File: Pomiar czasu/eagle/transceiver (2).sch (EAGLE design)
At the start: 64 parts, among them IC1 MEGA8-AI, IC2 LF33, IC3 LF50, U1 RFM69HW

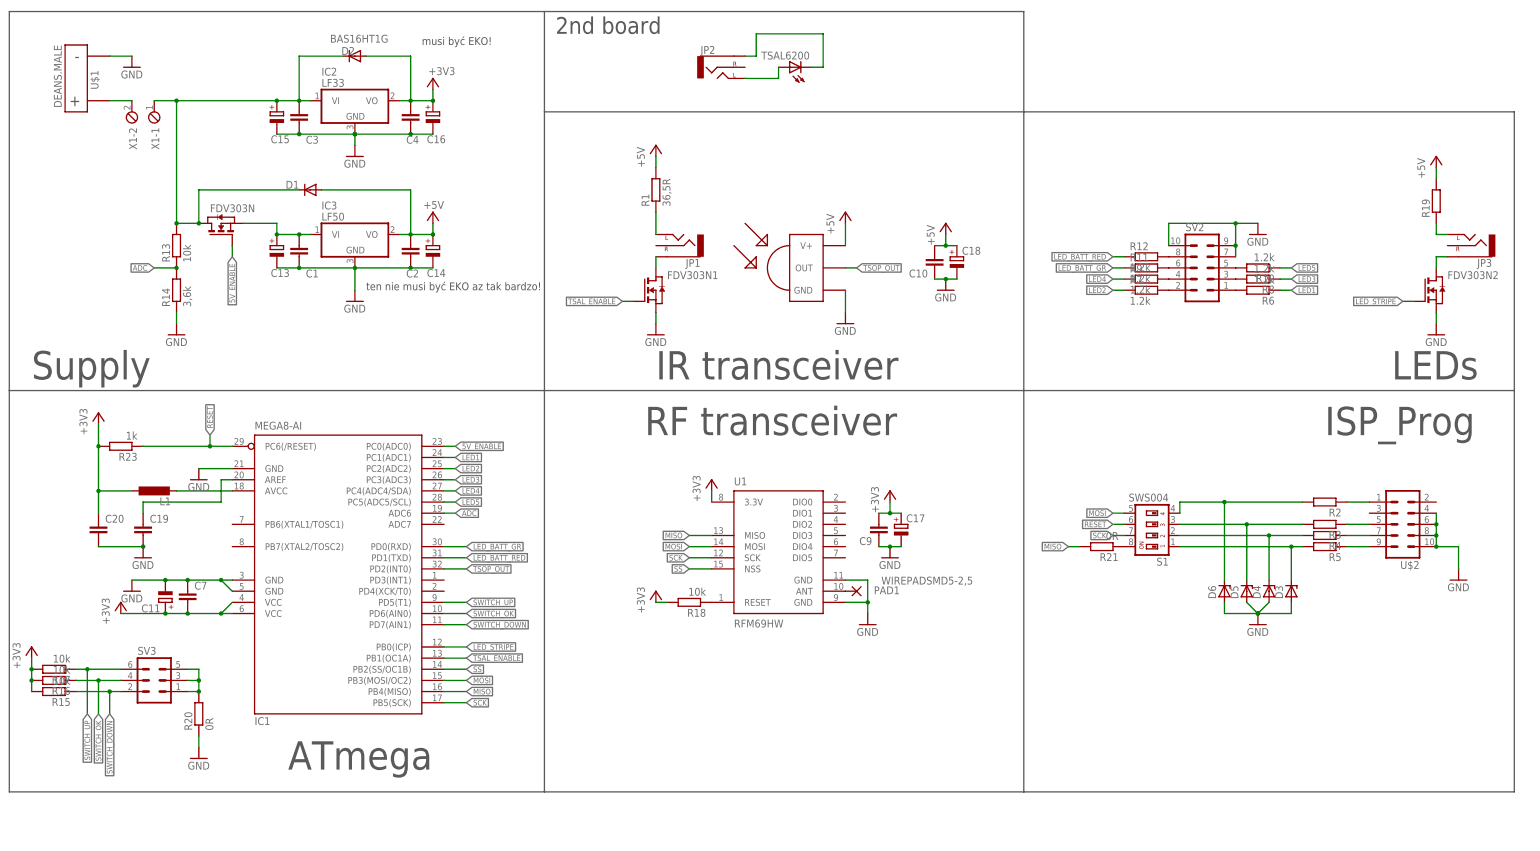
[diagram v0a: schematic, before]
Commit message: RFM69:communication master->sensor works!
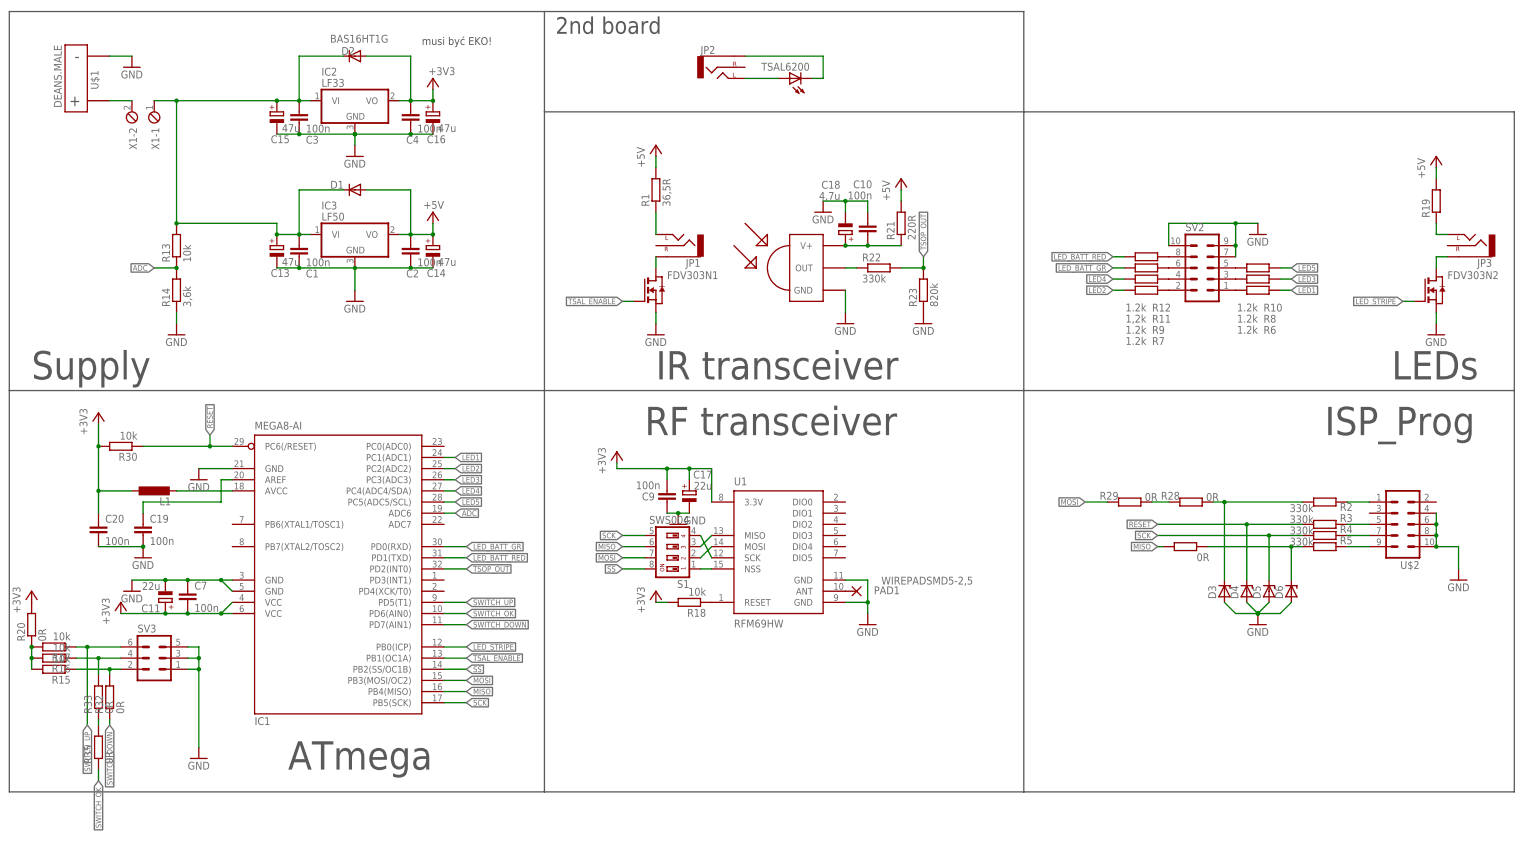
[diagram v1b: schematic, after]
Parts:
- removed FDV303N: (no value), zetex:NMOSSOT23
- added R22: 330k, resistor:R-EU_R0805
- added R28, R29, R31, R32, R33, R35: 0R, rcl:R-EU_R1206
- added R30: 10k, resistor:R-EU_R0805
- C1, C10, C19, C2, C20, C3, C4, C7, C9: value (none) -> 100n
- C11, C17: value (none) -> 22u
- C13, C14, C15, C16: value (none) -> 47u
- C18: value (none) -> 4,7u
- R2, R3, R4, R5: value (none) -> 330k
- R21: value 0R -> 220R; device rcl:R-EU_R1206 -> resistor:R-EU_R0805
- R23: value 1k -> 820k
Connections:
- removed net 5V_ENABLE: FDV303N.G, IC1.PC0(ADC0)
- removed net N$24: R21.1, S1.8
- new net N$25: C10.1, C18.+, R21.1, TSOP.V+
- new net N$33: R16.1, R33.2, SV3.4
- new net N$35: R33.1, R35.2
- new net N$36: S1.3, U1.MISO
- new net N$37: S1.2, U1.MOSI
- new net N$38: S1.4, U1.SCK
- new net N$39: S1.1, U1.NSS
- net +3V3: now also R20.2, R30.2; no longer R15.2, R16.2, R17.2, R23.2
- net +5V: now also R21.2; no longer C10.2, C18.+, TSOP.V+
- net GND: now also C10.2, R23.1, SV3.1, SV3.3, SV3.5; no longer C10.1, R20.1
- net MISO: now also R31.2, S1.6; no longer R21.2, U1.MISO
- net MOSI: now also R29.2, S1.7; no longer S1.5, U1.MOSI
- net N$1: now also R22.1, TSOP.OUT; no longer C1.1, C13.+, FDV303N.S, IC3.VI
- net N$23: now also R15.2, R16.2, R17.2, R20.1; no longer R20.2, SV3.1, SV3.3, SV3.5
- net N$27: now also C1.1, C13.+, IC3.VI; no longer FDV303N.D
- net N$29: now also R28.2, R29.1; no longer D6.C, R2.2, S1.4
- net N$30: now also D3.C, R2.2, R28.1; no longer D5.C, R3.2, S1.3
- net N$31: now also D6.C, R31.1, R5.2; no longer D4.C, R4.2, S1.2
- net N$32: now also R15.1, R32.2, SV3.2; no longer D3.C, R5.2, S1.1
- net RESET: now also D4.C, R3.2, R30.1; no longer R23.1, S1.6
- net SCK: now also D5.C, R4.2, S1.5; no longer S1.7, U1.SCK
- net SS: now also S1.8; no longer U1.NSS
- net SWITCH_DOWN: now also R32.1; no longer R15.1, SV3.2
- net SWITCH_OK: now also R35.1; no longer R16.1, SV3.4
- net TSOP_OUT: now also R22.2, R23.2; no longer TSOP.OUT
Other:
- note removed: "ten nie musi być EKO az tak bardzo!"
- moved on the sheet: C10, C17, C18, C9, D1, D3, D4, D5, D6, R15, R16, R17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

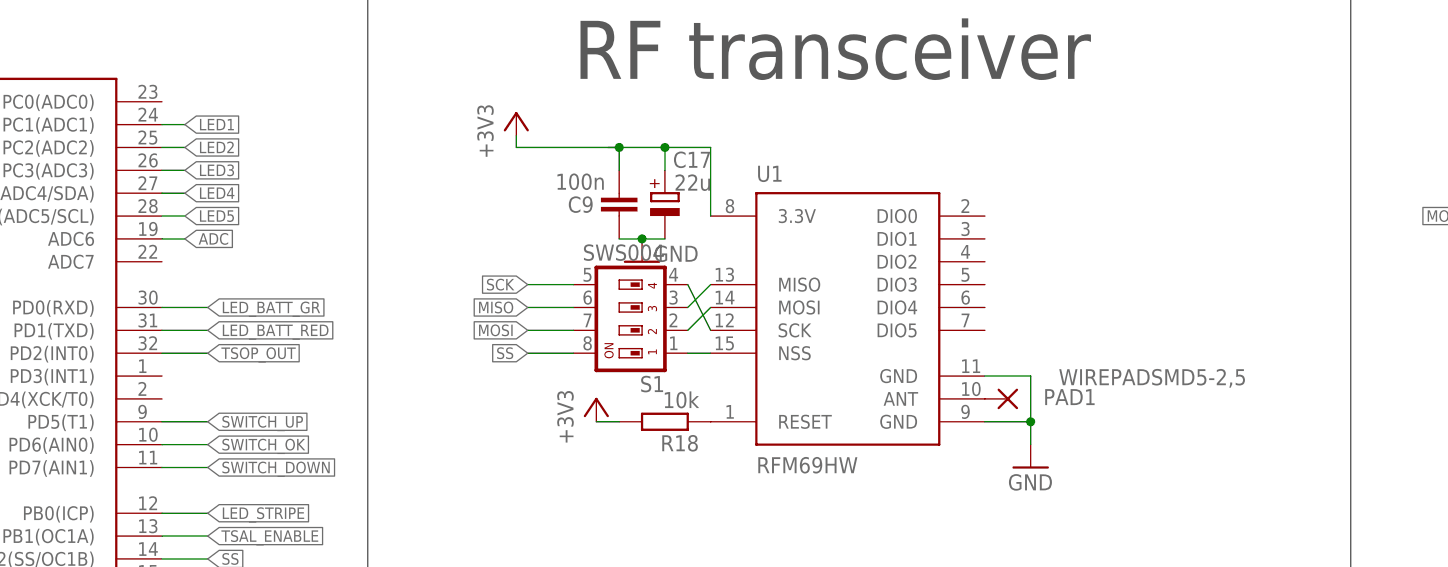
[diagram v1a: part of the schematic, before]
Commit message: Channel: 442MHz(!!), ping with acknowledgement
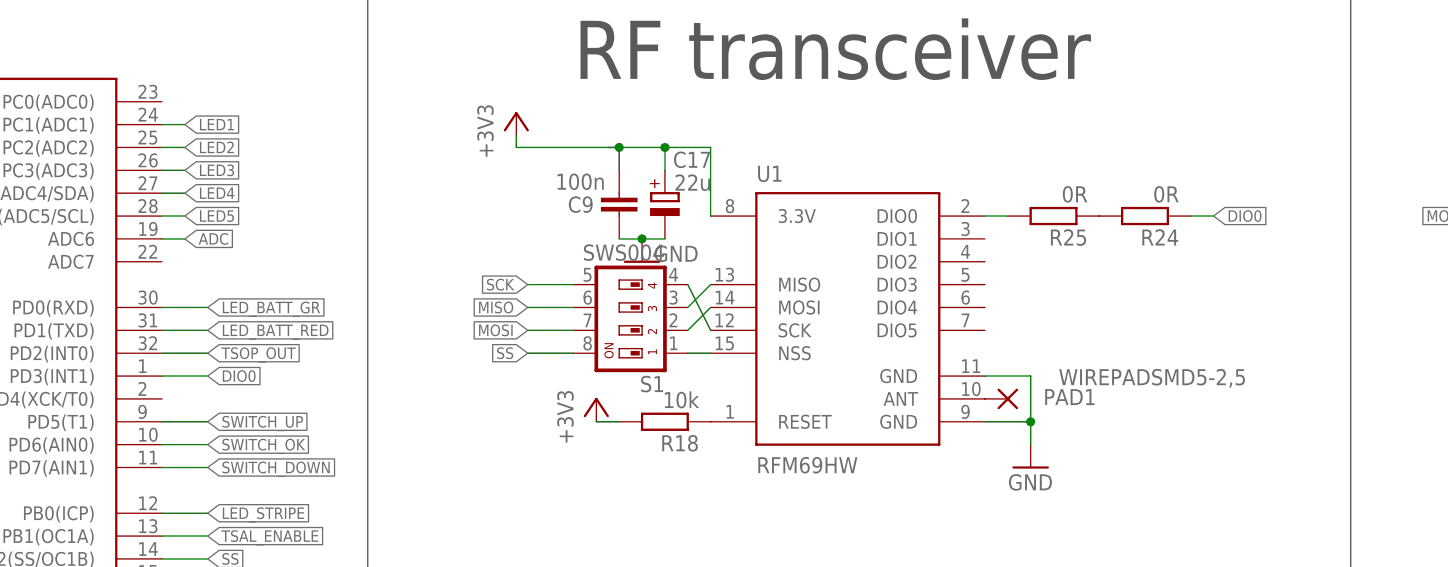
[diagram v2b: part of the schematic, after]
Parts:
- added R24, R25: 0R, rcl:R-EU_R1206
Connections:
- new net DIO0: IC1.PD3(INT1), R24.1
- new net N$24: R24.2, R25.1
- new net N$45: R25.2, U1.DIO0
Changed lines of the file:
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@@
 <part name="D6" library="diode" deviceset="ZENER-DIODE" device="SOD80C"/>
 <part name="S1" library="smd-special" deviceset="SWS004" device=""/>
+<part name="R24" library="rcl" deviceset="R-EU_" device="R1206" value="0R"/>
+<part name="R25" library="rcl" deviceset="R-EU_" device="R1206" value="0R"/>
 </parts>
 <sheets>
@@
 <instance part="D6" gate="G$1" x="299.72" y="48.26" rot="R90"/>
 <instance part="S1" gate="G$1" x="160.02" y="55.88" rot="R90"/>
+<instance part="R24" gate="G$1" x="215.9" y="68.58" rot="R180"/>
+<instance part="R25" gate="G$1" x="205.74" y="68.58" rot="R180"/>
 </instances>
 <busses>
@@
 </segment>
 </net>
+<net name="DIO0" class="0">
+<segment>
+<pinref part="IC1" gate="G$1" pin="PD3(INT1)"/>
+<wire x1="106.68" y1="50.8" x2="111.76" y2="50.8" width="0.1524" layer="91"/>
+<label x="111.76" y="50.8" size="1.27" layer="95" xref="yes"/>
+</segment>
+<segment>
+<pinref part="R24" gate="G$1" pin="1"/>
+<wire x1="220.98" y1="68.58" x2="223.52" y2="68.58" width="0.1524" layer="91"/>
+<label x="223.52" y="68.58" size="1.27" layer="95" xref="yes"/>
+</segment>
+</net>
+<net name="N$24" class="0">
+<segment>
+<pinref part="R25" gate="G$1" pin="1"/>
+<pinref part="R24" gate="G$1" pin="2"/>
+</segment>
+</net>
+<net name="N$45" class="0">
+<segment>
+<pinref part="U1" gate="G$1" pin="DIO0"/>
+<wire x1="198.12" y1="68.58" x2="200.66" y2="68.58" width="0.1524" layer="91"/>
+<pinref part="R25" gate="G$1" pin="2"/>
+</segment>
+</net>

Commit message: final v1.0
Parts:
- removed R23: 820k, resistor:R-EU_R0805
- added D7: (no value), diode:ZENER-DIODESOD80C
- R40: value 330k -> 220R
- renumbered R22 to R40
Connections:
- net +5V: now also JP1.LEFT; no longer R1.2
- net GND: now also D7.A; no longer R23.1
- net N$3: now also R1.2; no longer TSAL6200.A
- net N$8: now also TSAL6200.A; no longer JP1.LEFT
- net TSOP_OUT: now also D7.C; no longer R23.2
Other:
- moved on the sheet: R1, TSAL6200
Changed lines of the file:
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@@
 <setting verticaltext="up"/>
 </settings>
-<grid distance="0.05" unitdist="inch" unit="inch" style="lines" multiple="1" display="no" altdistance="0.01" altunitdist="inch" altunit="inch"/>
+<grid distance="0.1" unitdist="inch" unit="inch" style="lines" multiple="1" display="no" altdistance="0.01" altunitdist="inch" altunit="inch"/>
 <layers>
 <layer number="1" name="Top" color="4" fill="1" visible="no" active="no"/>
@@
 <part name="X1" library="con-phoenix-254" deviceset="MPT2" device=""/>
 <part name="R20" library="rcl" deviceset="R-EU_" device="R1206" value="0R"/>
-<part name="R22" library="resistor" deviceset="R-EU_" device="R0805" value="330k"/>
+<part name="R40" library="resistor" deviceset="R-EU_" device="R0805" value="220R"/>
 <part name="GND9" library="supply1" deviceset="GND" device=""/>
 <part name="R21" library="resistor" deviceset="R-EU_" device="R0805" value="220R"/>
 <part name="GND10" library="supply1" deviceset="GND" device=""/>
-<part name="R23" library="resistor" deviceset="R-EU_" device="R0805" value="820k"/>
 <part name="GND11" library="supply1" deviceset="GND" device=""/>
 <part name="R28" library="rcl" deviceset="R-EU_" device="R1206" value="0R"/>
@@
 <part name="R24" library="rcl" deviceset="R-EU_" device="R1206" value="0R"/>
 <part name="R25" library="rcl" deviceset="R-EU_" device="R1206" value="0R"/>
+<part name="D7" library="diode" deviceset="ZENER-DIODE" device="SOD80C"/>
 </parts>
 <sheets>
@@
 <instance part="+3V3" gate="G$1" x="33.02" y="45.72"/>
 <instance part="GND3" gate="1" x="35.56" y="48.26"/>
-<instance part="TSAL6200" gate="G$1" x="185.42" y="165.1" rot="R90"/>
+<instance part="TSAL6200" gate="G$1" x="193.04" y="165.1" rot="R90"/>
 <instance part="P+2" gate="1" x="210.82" y="142.24"/>
 <instance part="GND4" gate="1" x="198.12" y="109.22"/>
-<instance part="R1" gate="G$1" x="154.94" y="139.7" rot="R90"/>
+<instance part="R1" gate="G$1" x="182.88" y="165.1" rot="R180"/>
 <instance part="GND5" gate="1" x="154.94" y="106.68"/>
 <instance part="U1" gate="G$1" x="182.88" y="55.88"/>
@@
 <instance part="X1" gate="-2" x="35.56" y="157.48" rot="R270"/>
 <instance part="R20" gate="G$1" x="12.7" y="40.64" rot="R90"/>
-<instance part="R22" gate="G$1" x="205.74" y="121.92"/>
+<instance part="R40" gate="G$1" x="205.74" y="121.92"/>
 <instance part="GND9" gate="1" x="215.9" y="109.22"/>
 <instance part="R21" gate="G$1" x="210.82" y="132.08" rot="R90"/>
 <instance part="GND10" gate="1" x="193.04" y="134.62"/>
-<instance part="R23" gate="G$1" x="215.9" y="116.84" rot="R90"/>
 <instance part="GND11" gate="1" x="160.02" y="63.5" smashed="yes">
 <attribute name="VALUE" x="161.29" y="63.5" size="1.778" layer="96"/>
@@
 <instance part="R24" gate="G$1" x="215.9" y="68.58" rot="R180"/>
 <instance part="R25" gate="G$1" x="205.74" y="68.58" rot="R180"/>
+<instance part="D7" gate="G$1" x="215.9" y="116.84" rot="R90"/>
 </instances>
 <busses>
@@
 <pinref part="R19" gate="G$1" pin="2"/>
 <wire x1="332.74" y1="142.24" x2="332.74" y2="144.78" width="0.1524" layer="91"/>
-</segment>
-<segment>
-<pinref part="P+3" gate="1" pin="+5V"/>
-<pinref part="R1" gate="G$1" pin="2"/>
-<wire x1="154.94" y1="144.78" x2="154.94" y2="147.32" width="0.1524" layer="91"/>
 </segment>
 <segment>
@@
 <pinref part="P+2" gate="1" pin="+5V"/>
 <wire x1="210.82" y1="139.7" x2="210.82" y2="137.16" width="0.1524" layer="91"/>
+</segment>
+<segment>
+<pinref part="P+3" gate="1" pin="+5V"/>
+<pinref part="JP1" gate="G$1" pin="LEFT"/>
+<wire x1="154.94" y1="147.32" x2="154.94" y2="129.54" width="0.1524" layer="91"/>
 </segment>
 </net>
@@
 <segment>
 <label x="215.9" y="124.46" size="1.27" layer="95" rot="R90" xref="yes"/>
-<pinref part="R22" gate="G$1" pin="2"/>
+<pinref part="R40" gate="G$1" pin="2"/>
 <wire x1="215.9" y1="121.92" x2="215.9" y2="124.46" width="0.1524" layer="91"/>
 <wire x1="215.9" y1="121.92" x2="210.82" y2="121.92" width="0.1524" layer="91"/>
-<pinref part="R23" gate="G$1" pin="2"/>
+<pinref part="D7" gate="G$1" pin="C"/>
+<wire x1="215.9" y1="119.38" x2="215.9" y2="121.92" width="0.1524" layer="91"/>
 <junction x="215.9" y="121.92"/>
 </segment>
@@
 <net name="N$22" class="0">
 <segment>
-<wire x1="175.26" y1="170.18" x2="193.04" y2="170.18" width="0.1524" layer="91"/>
-<wire x1="193.04" y1="170.18" x2="193.04" y2="165.1" width="0.1524" layer="91"/>
+<wire x1="175.26" y1="170.18" x2="200.66" y2="170.18" width="0.1524" layer="91"/>
+<wire x1="200.66" y1="170.18" x2="200.66" y2="165.1" width="0.1524" layer="91"/>
 <pinref part="TSAL6200" gate="G$1" pin="C"/>
-<wire x1="193.04" y1="165.1" x2="190.5" y2="165.1" width="0.1524" layer="91"/>
+<wire x1="200.66" y1="165.1" x2="198.12" y2="165.1" width="0.1524" layer="91"/>
 <pinref part="JP2" gate="G$1" pin="SLEEVE"/>
 </segment>
@@
 </segment>
 </net>
-<net name="N$8" class="0">
-<segment>
-<pinref part="R1" gate="G$1" pin="1"/>
-<pinref part="JP1" gate="G$1" pin="LEFT"/>
-<wire x1="154.94" y1="134.62" x2="154.94" y2="129.54" width="0.1524" layer="91"/>
-</segment>
-</net>
 <net name="N$14" class="0">
 <segment>
@@
 </segment>
 <segment>
-<pinref part="R23" gate="G$1" pin="1"/>
-<pinref part="GND9" gate="1" pin="GND"/>
-</segment>
-<segment>
 <wire x1="284.48" y1="45.72" x2="287.02" y2="43.18" width="0.1524" layer="91"/>
 <pinref part="GND8" gate="1" pin="GND"/>
@@
 <junction x="160.02" y="66.04"/>
 </segment>
+<segment>
+<pinref part="D7" gate="G$1" pin="A"/>
+<pinref part="GND9" gate="1" pin="GND"/>
+<wire x1="215.9" y1="114.3" x2="215.9" y2="111.76" width="0.1524" layer="91"/>
+</segment>
 </net>
 <net name="N$15" class="0">
@@
 </segment>
 </net>
-<net name="N$3" class="0">
-<segment>
-<pinref part="JP2" gate="G$1" pin="LEFT"/>
-<pinref part="TSAL6200" gate="G$1" pin="A"/>
-<wire x1="175.26" y1="165.1" x2="182.88" y2="165.1" width="0.1524" layer="91"/>
-</segment>
-</net>
 <net name="N$1" class="0">
 <segment>
 <pinref part="TSOP" gate="G$1" pin="OUT"/>
-<pinref part="R22" gate="G$1" pin="1"/>
+<pinref part="R40" gate="G$1" pin="1"/>
 <wire x1="200.66" y1="121.92" x2="198.12" y2="121.92" width="0.1524" layer="91"/>
 </segment>
@@
 </segment>
 </net>
+<net name="N$3" class="0">
+<segment>
+<pinref part="JP2" gate="G$1" pin="LEFT"/>
+<pinref part="R1" gate="G$1" pin="2"/>
+<wire x1="177.8" y1="165.1" x2="175.26" y2="165.1" width="0.1524" layer="91"/>
+</segment>
+</net>
+<net name="N$8" class="0">
+<segment>
+<pinref part="TSAL6200" gate="G$1" pin="A"/>
+<pinref part="R1" gate="G$1" pin="1"/>
+<wire x1="187.96" y1="165.1" x2="190.5" y2="165.1" width="0.1524" layer="91"/>
+</segment>
+</net>
